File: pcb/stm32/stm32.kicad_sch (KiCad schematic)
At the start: 9 parts, among them J12 Conn_01x02_Pin, U1 24AA02-OT, U2 23A256, U3 TPS2041B

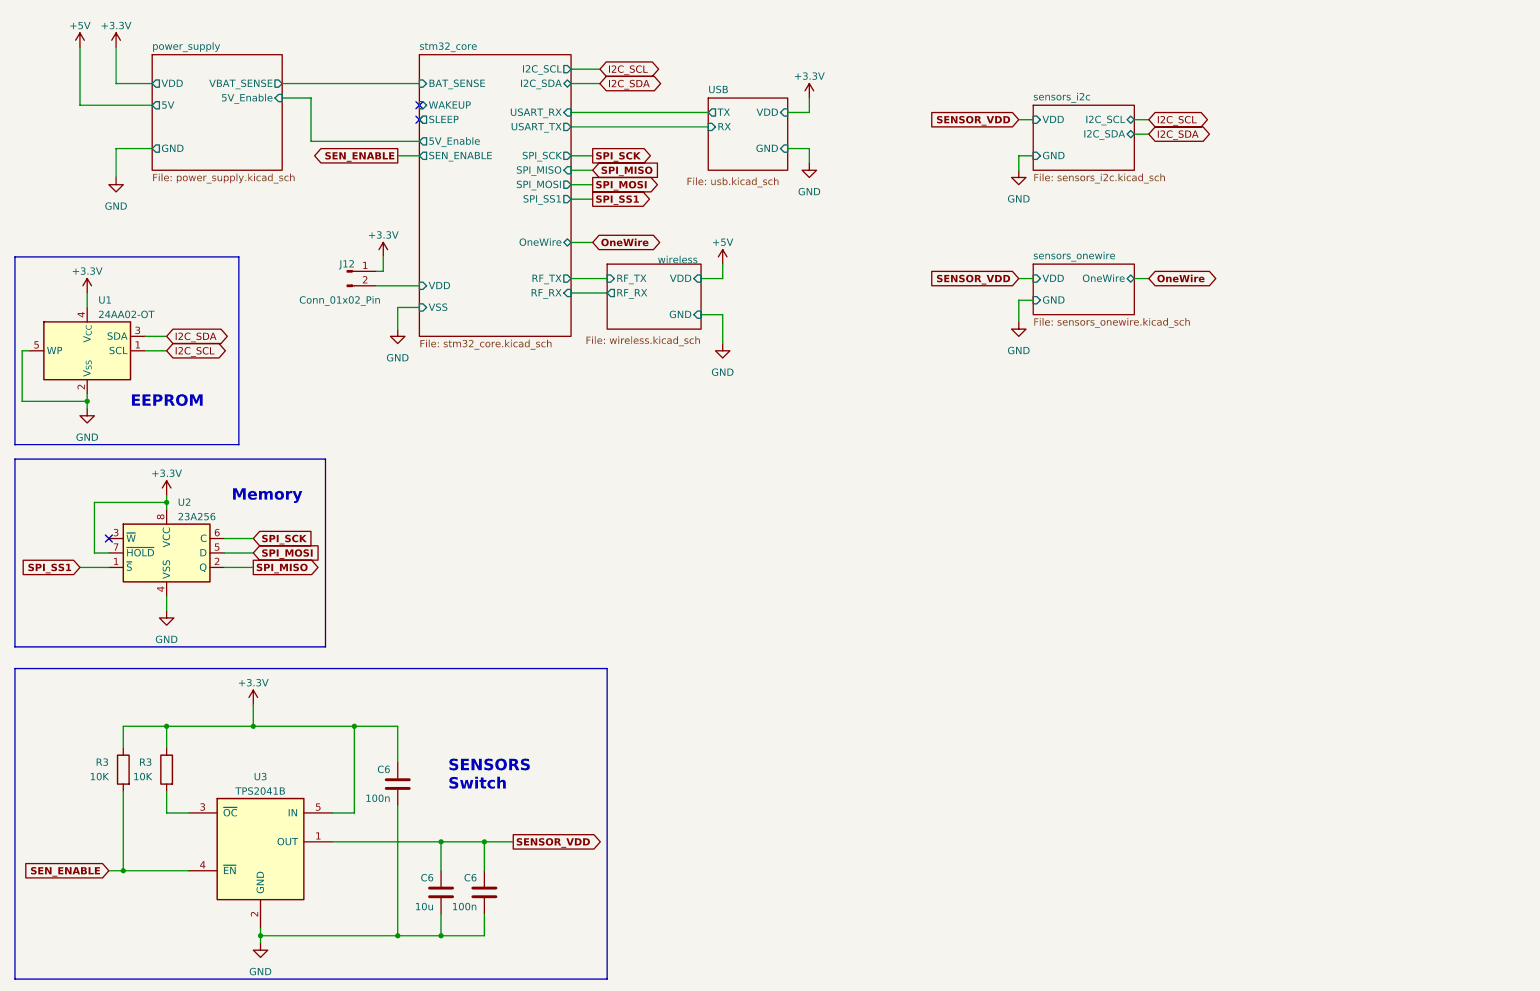
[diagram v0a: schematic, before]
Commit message: VDD supply added
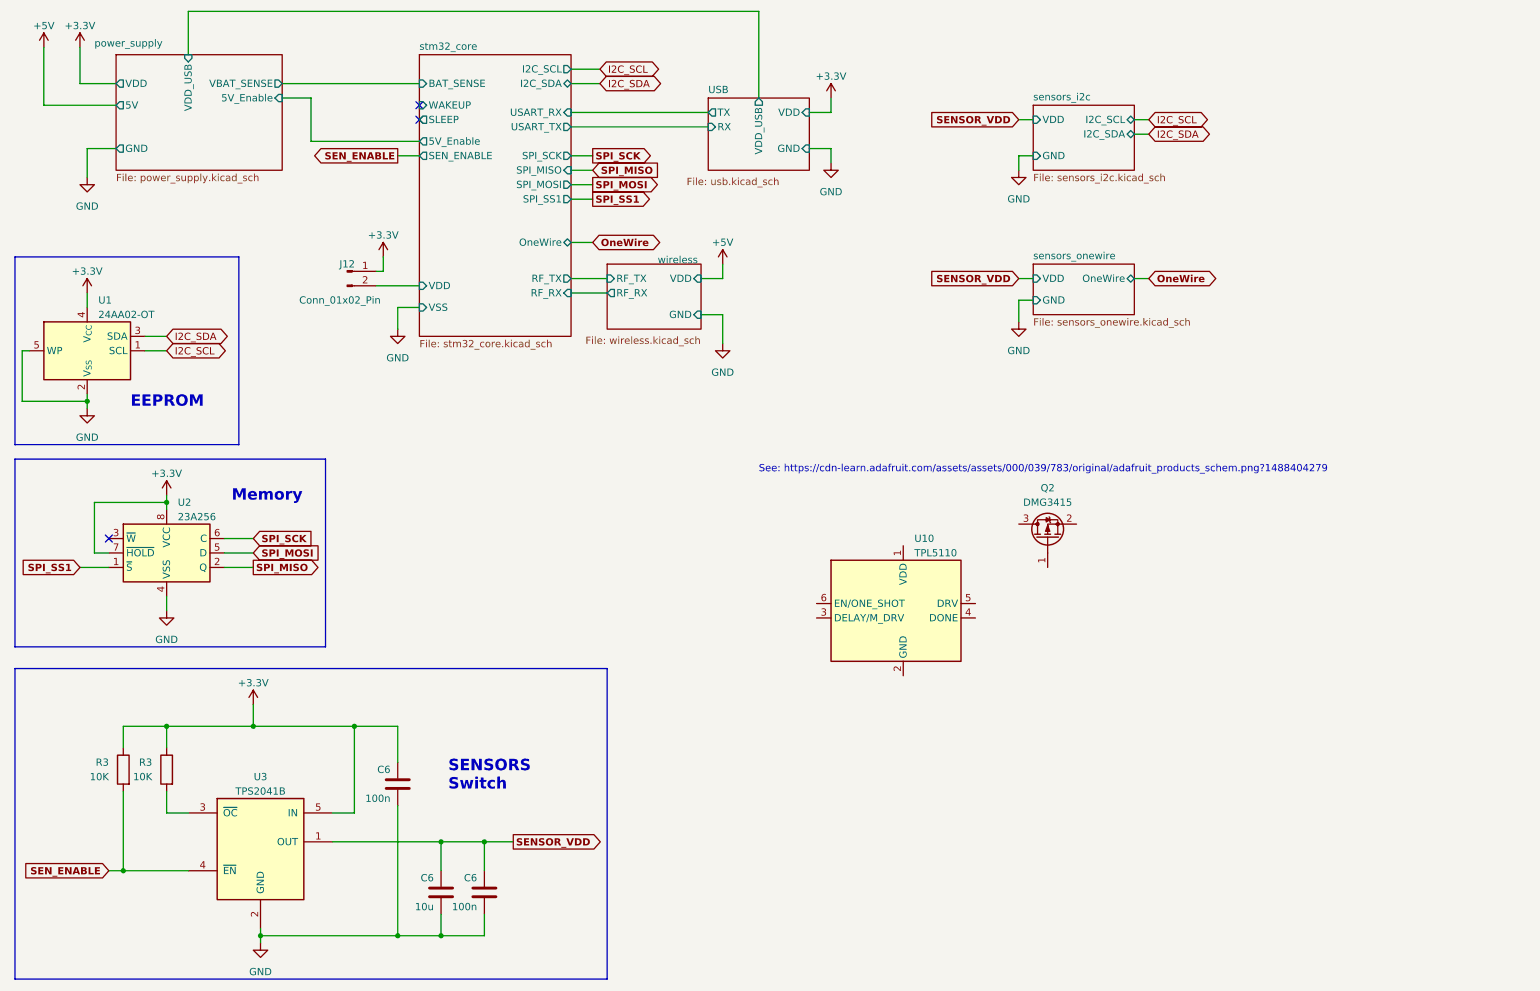
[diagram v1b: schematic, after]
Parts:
- added Q2: DMG3415, Package_TO_SOT_SMD:SOT-23, symbol Transistor_FET:DMG2301L
- added U10: TPL5110, Package_TO_SOT_SMD:SOT-23-6, symbol Timer:TPL5110
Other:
- sheet USB ports: added VDD_USB; removed none
- sheet power_supply ports: added VDD_USB; removed none
- note added: "See: https://cdn-learn.adafruit.com/assets/assets/000/039/783/original/adafruit_products_schem.png?1488404279"

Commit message: WIP pcb
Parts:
- removed Q2: DMG3415, Package_TO_SOT_SMD:SOT-23, symbol Transistor_FET:DMG2301L
- removed U10: TPL5110, Package_TO_SOT_SMD:SOT-23-6, symbol Timer:TPL5110
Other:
- note removed: "See: https://cdn-learn.adafruit.com/assets/assets/000/039/783/original/adafruit_products_schem.png?1488404279"
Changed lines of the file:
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@@
     (effects (font (size 2 2) bold) (justify left bottom))
-  )
-  (text "See: https://cdn-learn.adafruit.com/assets/assets/000/039/783/original/adafruit_products_schem.png?1488404279"
-    (at 146.05 105.41 0)
-    (effects (font (size 1.27 1.27)) (justify left bottom))
   )
   (global_label "SPI_MOSI" (shape input) (at 57.15 119.38 0) (fields_autoplaced)
@@
         (path "/cc56704c-71b4-401e-bec6-203f83946289"
           (reference "#PWR017") (unit 1)
-        )
-      )
-    )
-  )
-  (symbol (lib_id "Transistor_FET:DMG2301L") (at 196.85 116.84 90) (unit 1)
-    (in_bom yes) (on_board yes) (dnp no) (fields_autoplaced)
-    (property "Reference" "Q2" (at 196.85 107.95 90)
-      (effects (font (size 1.27 1.27)))
-    )
-    (property "Value" "DMG3415" (at 196.85 110.49 90)
-      (effects (font (size 1.27 1.27)))
-    )
-    (property "Footprint" "Package_TO_SOT_SMD:SOT-23" (at 198.755 111.76 0)
-      (effects (font (size 1.27 1.27) italic) (justify left) hide)
-    )
-    (property "Datasheet" "https://www.diodes.com/assets/Datasheets/DMG2301L.pdf" (at 196.85 116.84 0)
-      (effects (font (size 1.27 1.27)) (justify left) hide)
-    )
-    (pin "1")
-    (pin "2")
-    (pin "3")
-    (instances
-      (project "stm32"
-        (path "/cc56704c-71b4-401e-bec6-203f83946289"
-          (reference "Q2") (unit 1)
         )
       )
@@
         )
       )
-    )
-  )
-  (symbol (lib_id "Timer:TPL5110") (at 171.45 128.27 0) (unit 1)
-    (in_bom yes) (on_board yes) (dnp no) (fields_autoplaced)
-    (property "Reference" "U10" (at 173.4059 116.84 0)
-      (effects (font (size 1.27 1.27)) (justify left))
-    )
-    (property "Value" "TPL5110" (at 173.4059 119.38 0)
-      (effects (font (size 1.27 1.27)) (justify left))
-    )
-    (property "Footprint" "Package_TO_SOT_SMD:SOT-23-6" (at 171.45 128.27 0)
-      (effects (font (size 1.27 1.27)) hide)
-    )
-    (property "Datasheet" "http://www.ti.com/lit/ds/symlink/tpl5110.pdf" (at 166.37 138.43 0)
-      (effects (font (size 1.27 1.27)) hide)
-    )
-    (pin "1")
-    (pin "2")
-    (pin "3")
-    (pin "4")
-    (pin "5")
-    (pin "6")
-    (instances
-      (project "stm32"
-        (path "/cc56704c-71b4-401e-bec6-203f83946289"
-          (reference "U10") (unit 1)
-        )
-      )

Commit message: Added todos
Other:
- note added: "TODO:Try adding place for breadboard TODO: EPS32"
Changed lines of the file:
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@@
     (fill (type none))
+  )
+  (text "TODO:Try adding place for breadboard\nTODO: EPS32" (at 127 120.65 0)
+    (effects (font (size 3 3)) (justify left bottom))
   )
   (text "Memory" (at 53.34 110.49 0)

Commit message: update
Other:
- note added: "TODO: header?"
- note removed: "TODO:Try adding place for breadboard TODO: EPS32"
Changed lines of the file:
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@@
     (fill (type none))
-  )
-  (text "TODO:Try adding place for breadboard\nTODO: EPS32" (at 127 120.65 0)
-    (effects (font (size 3 3)) (justify left bottom))
   )
   (text "Memory" (at 53.34 110.49 0)
@@
     (effects (font (size 2 2) bold) (justify left bottom))
   )
+  (text "TODO: header?" (at 71.12 43.18 0)
+    (effects (font (size 1.27 1.27)) (justify left bottom))
+  )
   (global_label "SPI_MOSI" (shape input) (at 57.15 119.38 0) (fields_autoplaced)
